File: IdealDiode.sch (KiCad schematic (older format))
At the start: 5 parts, among them Q27 MBT3906DW1, Q28 SQ3493EV

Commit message: Adapt 2590 board layout to ideal diodes and dual power input connector
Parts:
- Q27: footprint TO_SOT_Packages_SMD:SOT-363_SC-70-6 -> Package_TO_SOT_SMD:SOT-363_SC-70-6
- Q28: footprint Housings_SSOP:TSOP-6_1.65x3.05mm_Pitch0.95mm -> Package_SO:TSOP-6_1.65x3.05mm_P0.95mm; symbol SQ3493EV:SQ3493EV -> smoothiev2-prime-rescue:SQ3493EV-SQ3493EV
- R105, R106, R107: footprint Resistors_SMD:R_0402 -> Resistor_SMD:R_0402_1005Metric
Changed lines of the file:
@@
 Comment4 ""
 $EndDescr
-$Comp
-L Transistor_BJT:MBT3906DW1 Q27
-U 1 1 63884AE6
-P 2425 2500
-AR Path="/631D7D17/63881870/63884AE6" Ref="Q27"  Part="1"
-AR Path="/631D7D17/638DB850/63884AE6" Ref="Q29"  Part="1"
-AR Path="/631D7D17/638DE946/63884AE6" Ref="Q31"  Part="1"
-F 0 "Q31" H 2616 2454 50  0000 L CNN
-F 1 "MBT3906DW1" H 2616 2545 50  0000 L CNN
-F 2 "TO_SOT_Packages_SMD:SOT-363_SC-70-6" H 2625 2600 50  0001 C CNN
-F 3 "http://www.onsemi.com/pub_link/Collateral/MBT3906DW1T1-D.PDF" H 2425 2500 50  0001 C CNN
-	1    2425 2500
-	-1   0    0    1
-$EndComp
-$Comp
-L Transistor_BJT:MBT3906DW1 Q27
-U 2 1 6388718E
-P 2825 2500
-AR Path="/631D7D17/63881870/6388718E" Ref="Q27"  Part="2"
-AR Path="/631D7D17/638DB850/6388718E" Ref="Q29"  Part="2"
-AR Path="/631D7D17/638DE946/6388718E" Ref="Q31"  Part="2"
-F 0 "Q31" H 3015 2454 50  0000 L CNN
-F 1 "MBT3906DW1" H 3015 2545 50  0000 L CNN
-F 2 "TO_SOT_Packages_SMD:SOT-363_SC-70-6" H 3025 2600 50  0001 C CNN
-F 3 "http://www.onsemi.com/pub_link/Collateral/MBT3906DW1T1-D.PDF" H 2825 2500 50  0001 C CNN
-	2    2825 2500
-	1    0    0    1
-$EndComp
 Wire Wire Line
 	2625 2500 2625 2700
@@
 AR Path="/631D7D17/638DB850/638894E4" Ref="R108"  Part="1"
 AR Path="/631D7D17/638DE946/638894E4" Ref="R111"  Part="1"
-F 0 "R111" H 2384 2846 50  0000 L CNN
+F 0 "R105" H 2384 2846 50  0000 L CNN
 F 1 "10k" H 2384 2755 50  0000 L CNN
-F 2 "Resistors_SMD:R_0402" H 2325 2800 50  0001 C CNN
+F 2 "Resistor_SMD:R_0402_1005Metric" H 2325 2800 50  0001 C CNN
 F 3 "~" H 2325 2800 50  0001 C CNN
 	1    2325 2800
@@
 AR Path="/631D7D17/638DB850/63889C41" Ref="R109"  Part="1"
 AR Path="/631D7D17/638DE946/63889C41" Ref="R112"  Part="1"
-F 0 "R112" H 2684 2846 50  0000 L CNN
+F 0 "R106" H 2684 2846 50  0000 L CNN
 F 1 "100k" H 2684 2755 50  0000 L CNN
-F 2 "Resistors_SMD:R_0402" H 2625 2800 50  0001 C CNN
+F 2 "Resistor_SMD:R_0402_1005Metric" H 2625 2800 50  0001 C CNN
 F 3 "~" H 2625 2800 50  0001 C CNN
 	1    2625 2800
@@
 AR Path="/631D7D17/638DB850/63889F07" Ref="R110"  Part="1"
 AR Path="/631D7D17/638DE946/63889F07" Ref="R113"  Part="1"
-F 0 "R113" H 2984 2846 50  0000 L CNN
+F 0 "R107" H 2984 2846 50  0000 L CNN
 F 1 "10k" H 2984 2755 50  0000 L CNN
-F 2 "Resistors_SMD:R_0402" H 2925 2800 50  0001 C CNN
+F 2 "Resistor_SMD:R_0402_1005Metric" H 2925 2800 50  0001 C CNN
 F 3 "~" H 2925 2800 50  0001 C CNN
 	1    2925 2800
@@
 $EndComp
 $Comp
-L SQ3493EV:SQ3493EV Q28
+L smoothiev2-prime-rescue:SQ3493EV-SQ3493EV Q28
 U 1 1 6388DA58
 P 2625 2050
@@
 AR Path="/631D7D17/638DB850/6388DA58" Ref="Q30"  Part="1"
 AR Path="/631D7D17/638DE946/6388DA58" Ref="Q32"  Part="1"
-F 0 "Q32" H 2637 2565 50  0000 C CNN
+AR Path="/6388DA58" Ref="Q32"  Part="1"
+F 0 "Q28" H 2637 2565 50  0000 C CNN
 F 1 "SQ3493EV" H 2637 2474 50  0000 C CNN
-F 2 "Housings_SSOP:TSOP-6_1.65x3.05mm_Pitch0.95mm" H 2625 2050 50  0001 C CNN
+F 2 "Package_SO:TSOP-6_1.65x3.05mm_P0.95mm" H 2625 2050 50  0001 C CNN
 F 3 "" H 2625 2050 50  0001 C CNN
 	1    2625 2050
@@
 AR Path="/631D7D17/638DB850/638903FB" Ref="#PWR0154"  Part="1"
 AR Path="/631D7D17/638DE946/638903FB" Ref="#PWR0155"  Part="1"
-F 0 "#PWR0155" H 2625 2650 50  0001 C CNN
+F 0 "#PWR0153" H 2625 2650 50  0001 C CNN
 F 1 "GND" H 2630 2727 50  0000 C CNN
 F 2 "" H 2625 2900 50  0001 C CNN
@@
 Text HLabel 2925 2125 2    50   BiDi ~ 0
 ID_out
+$Comp
+L Transistor_BJT:MBT3906DW1 Q27
+U 1 1 63884AE6
+P 2425 2500
+AR Path="/631D7D17/63881870/63884AE6" Ref="Q27"  Part="1"
+AR Path="/631D7D17/638DB850/63884AE6" Ref="Q29"  Part="1"
+AR Path="/631D7D17/638DE946/63884AE6" Ref="Q31"  Part="1"
+F 0 "Q27" H 2616 2454 50  0000 L CNN
+F 1 "MBT3906DW1" H 2616 2545 50  0000 L CNN
+F 2 "Package_TO_SOT_SMD:SOT-363_SC-70-6" H 2625 2600 50  0001 C CNN
+F 3 "http://www.onsemi.com/pub_link/Collateral/MBT3906DW1T1-D.PDF" H 2425 2500 50  0001 C CNN
+	1    2425 2500
+	-1   0    0    1
+$EndComp
+$Comp
+L Transistor_BJT:MBT3906DW1 Q27
+U 2 1 6388718E
+P 2825 2500
+AR Path="/631D7D17/63881870/6388718E" Ref="Q27"  Part="2"
+AR Path="/631D7D17/638DB850/6388718E" Ref="Q29"  Part="2"
+AR Path="/631D7D17/638DE946/6388718E" Ref="Q31"  Part="2"
+F 0 "Q27" H 3015 2454 50  0000 L CNN
+F 1 "MBT3906DW1" H 3015 2545 50  0000 L CNN
+F 2 "Package_TO_SOT_SMD:SOT-363_SC-70-6" H 3025 2600 50  0001 C CNN
+F 3 "http://www.onsemi.com/pub_link/Collateral/MBT3906DW1T1-D.PDF" H 2825 2500 50  0001 C CNN
+	2    2825 2500
+	1    0    0    1
+$EndComp
 $EndSCHEMATC

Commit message: Updated 2660 version to match 2590 mods.
Updated 2660 version to match 2590 mods.  Ideal diodes, move board thermistor, add extra fet connector, modify probe input.
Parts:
- Q28: symbol smoothiev2-prime-rescue:SQ3493EV-SQ3493EV -> smoothiev2-prime-2660-rescue:SQ3493EV-SQ3493EV-smoothiev2-prime-rescue
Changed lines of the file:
@@
 $Descr A4 11693 8268
 encoding utf-8
-Sheet 11 13
+Sheet 7 13
 Title ""
 Date ""
@@
 AR Path="/631D7D17/638DB850/638894E4" Ref="R108"  Part="1"
 AR Path="/631D7D17/638DE946/638894E4" Ref="R111"  Part="1"
-F 0 "R105" H 2384 2846 50  0000 L CNN
+F 0 "R111" H 2384 2846 50  0000 L CNN
 F 1 "10k" H 2384 2755 50  0000 L CNN
 F 2 "Resistor_SMD:R_0402_1005Metric" H 2325 2800 50  0001 C CNN
@@
 AR Path="/631D7D17/638DB850/63889C41" Ref="R109"  Part="1"
 AR Path="/631D7D17/638DE946/63889C41" Ref="R112"  Part="1"
-F 0 "R106" H 2684 2846 50  0000 L CNN
+F 0 "R112" H 2684 2846 50  0000 L CNN
 F 1 "100k" H 2684 2755 50  0000 L CNN
 F 2 "Resistor_SMD:R_0402_1005Metric" H 2625 2800 50  0001 C CNN
@@
 AR Path="/631D7D17/638DB850/63889F07" Ref="R110"  Part="1"
 AR Path="/631D7D17/638DE946/63889F07" Ref="R113"  Part="1"
-F 0 "R107" H 2984 2846 50  0000 L CNN
+F 0 "R113" H 2984 2846 50  0000 L CNN
 F 1 "10k" H 2984 2755 50  0000 L CNN
 F 2 "Resistor_SMD:R_0402_1005Metric" H 2925 2800 50  0001 C CNN
@@
 $EndComp
 $Comp
-L smoothiev2-prime-rescue:SQ3493EV-SQ3493EV Q28
+L smoothiev2-prime-2660-rescue:SQ3493EV-SQ3493EV-smoothiev2-prime-rescue Q28
 U 1 1 6388DA58
 P 2625 2050
@@
 AR Path="/631D7D17/638DE946/6388DA58" Ref="Q32"  Part="1"
 AR Path="/6388DA58" Ref="Q32"  Part="1"
-F 0 "Q28" H 2637 2565 50  0000 C CNN
+F 0 "Q32" H 2637 2565 50  0000 C CNN
 F 1 "SQ3493EV" H 2637 2474 50  0000 C CNN
 F 2 "Package_SO:TSOP-6_1.65x3.05mm_P0.95mm" H 2625 2050 50  0001 C CNN
@@
 AR Path="/631D7D17/638DB850/63884AE6" Ref="Q29"  Part="1"
 AR Path="/631D7D17/638DE946/63884AE6" Ref="Q31"  Part="1"
-F 0 "Q27" H 2616 2454 50  0000 L CNN
+F 0 "Q31" H 2616 2454 50  0000 L CNN
 F 1 "MBT3906DW1" H 2616 2545 50  0000 L CNN
 F 2 "Package_TO_SOT_SMD:SOT-363_SC-70-6" H 2625 2600 50  0001 C CNN
@@
 AR Path="/631D7D17/638DB850/6388718E" Ref="Q29"  Part="2"
 AR Path="/631D7D17/638DE946/6388718E" Ref="Q31"  Part="2"
-F 0 "Q27" H 3015 2454 50  0000 L CNN
+F 0 "Q31" H 3015 2454 50  0000 L CNN
 F 1 "MBT3906DW1" H 3015 2545 50  0000 L CNN
 F 2 "Package_TO_SOT_SMD:SOT-363_SC-70-6" H 3025 2600 50  0001 C CNN

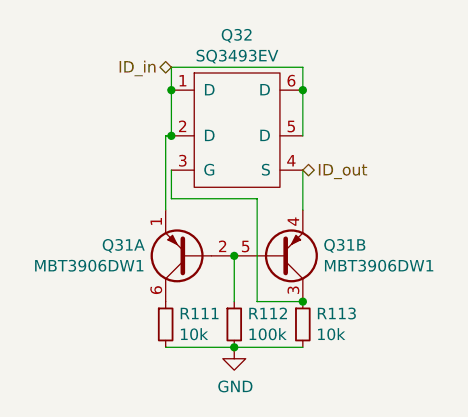
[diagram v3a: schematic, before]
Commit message: Fix most DRC errors Fix bulk traces for disconnect FET Fix silkscreen indicator for disconnect FET Add fiducials Bump version numbers (proto9 for 2660, proto10 for 2590)
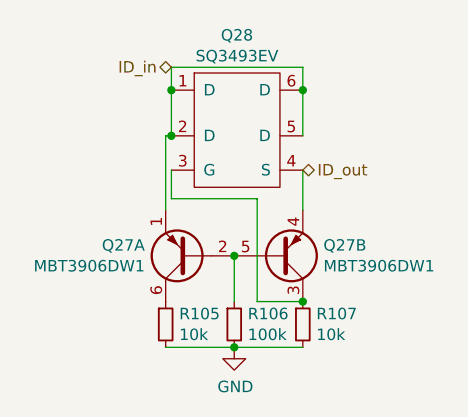
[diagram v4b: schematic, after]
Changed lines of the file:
@@
 AR Path="/631D7D17/638DB850/638894E4" Ref="R108"  Part="1"
 AR Path="/631D7D17/638DE946/638894E4" Ref="R111"  Part="1"
-F 0 "R111" H 2384 2846 50  0000 L CNN
+F 0 "R105" H 2384 2846 50  0000 L CNN
 F 1 "10k" H 2384 2755 50  0000 L CNN
 F 2 "Resistor_SMD:R_0402_1005Metric" H 2325 2800 50  0001 C CNN
@@
 AR Path="/631D7D17/638DB850/63889C41" Ref="R109"  Part="1"
 AR Path="/631D7D17/638DE946/63889C41" Ref="R112"  Part="1"
-F 0 "R112" H 2684 2846 50  0000 L CNN
+F 0 "R106" H 2684 2846 50  0000 L CNN
 F 1 "100k" H 2684 2755 50  0000 L CNN
 F 2 "Resistor_SMD:R_0402_1005Metric" H 2625 2800 50  0001 C CNN
@@
 AR Path="/631D7D17/638DB850/63889F07" Ref="R110"  Part="1"
 AR Path="/631D7D17/638DE946/63889F07" Ref="R113"  Part="1"
-F 0 "R113" H 2984 2846 50  0000 L CNN
+F 0 "R107" H 2984 2846 50  0000 L CNN
 F 1 "10k" H 2984 2755 50  0000 L CNN
 F 2 "Resistor_SMD:R_0402_1005Metric" H 2925 2800 50  0001 C CNN
@@
 AR Path="/631D7D17/638DE946/6388DA58" Ref="Q32"  Part="1"
 AR Path="/6388DA58" Ref="Q32"  Part="1"
-F 0 "Q32" H 2637 2565 50  0000 C CNN
+F 0 "Q28" H 2637 2565 50  0000 C CNN
 F 1 "SQ3493EV" H 2637 2474 50  0000 C CNN
 F 2 "Package_SO:TSOP-6_1.65x3.05mm_P0.95mm" H 2625 2050 50  0001 C CNN
@@
 AR Path="/631D7D17/638DB850/63884AE6" Ref="Q29"  Part="1"
 AR Path="/631D7D17/638DE946/63884AE6" Ref="Q31"  Part="1"
-F 0 "Q31" H 2616 2454 50  0000 L CNN
+F 0 "Q27" H 2616 2454 50  0000 L CNN
 F 1 "MBT3906DW1" H 2616 2545 50  0000 L CNN
 F 2 "Package_TO_SOT_SMD:SOT-363_SC-70-6" H 2625 2600 50  0001 C CNN
@@
 AR Path="/631D7D17/638DB850/6388718E" Ref="Q29"  Part="2"
 AR Path="/631D7D17/638DE946/6388718E" Ref="Q31"  Part="2"
-F 0 "Q31" H 3015 2454 50  0000 L CNN
+F 0 "Q27" H 3015 2454 50  0000 L CNN
 F 1 "MBT3906DW1" H 3015 2545 50  0000 L CNN
 F 2 "Package_TO_SOT_SMD:SOT-363_SC-70-6" H 3025 2600 50  0001 C CNN
